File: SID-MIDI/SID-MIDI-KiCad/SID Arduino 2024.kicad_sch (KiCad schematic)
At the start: 33 parts, among them J1 Power, J5 Audio, J9 MIDI, SW4 Reset, SW6 Unison/Poly/Separate, U1 TL072, U2 6N138, U3 MOS6581/6582/8580SID

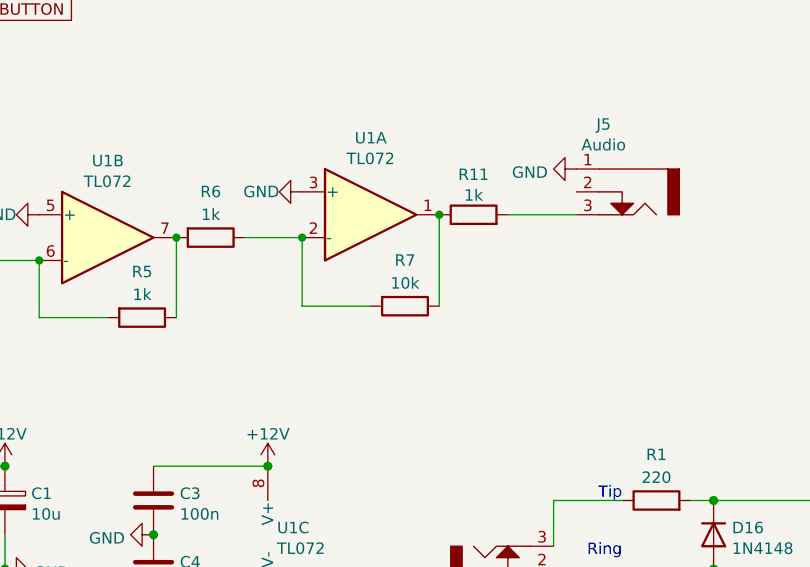
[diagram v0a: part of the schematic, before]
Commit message: Change amplification resistor to 1k8 to avoid clipping
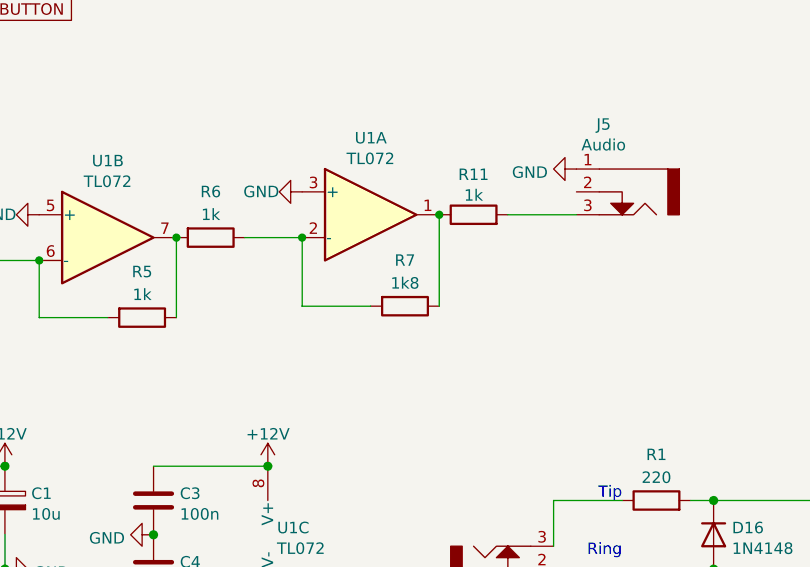
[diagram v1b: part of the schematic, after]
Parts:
- R7: value 10k -> 1k8
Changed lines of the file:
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@@
       (effects (font (size 1.27 1.27)))
     )
-    (property "Value" "10k" (at 88.9 147.32 90)
+    (property "Value" "1k8" (at 88.9 147.32 90)
       (effects (font (size 1.27 1.27)))
     )

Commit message: Add files via upload
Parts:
- R7: value 1k8 -> 1k
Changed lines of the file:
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@@
       (effects (font (size 1.27 1.27)))
     )
-    (property "Value" "1k8" (at 88.9 147.32 90)
+    (property "Value" "1k" (at 88.9 147.32 90)
       (effects (font (size 1.27 1.27)))
     )

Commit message: Add files via upload
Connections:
- net Poly/Unison 0: now also A1.1 (D1/TX); no longer A1.15 (D12)
- net SID DATA 1: now also A1.15 (D12); no longer A1.1 (D1/TX)
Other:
- note added: "The AMS1117 5.0V on the Arduino Nano should be able to supply at least 800mA, and the SID should draw about 100mA via Vcc, so this should be within safe limits, although the AMS1117 can get quite warm"
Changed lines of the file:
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@@
     (effects (font (size 1.27 1.27)) (justify right bottom))
+  )
+  (text "The AMS1117 5.0V on the Arduino Nano\nshould be able to supply at least 800mA,\nand the SID should draw about 100mA\nvia Vcc, so this should be within safe\nlimits, although the AMS1117 can get quite warm"
+    (at 166.37 49.53 0)
+    (effects (font (size 1.27 1.27)) (justify left bottom))
   )
   (text "D13: Important note:\nRemove resistor or LED from\nD13, to allow INPUT_PULLUP\nto work correctly"
@@
     )
   )
-  (global_label "Poly{slash}Unison 0" (shape input) (at 74.93 62.23 180) (fields_autoplaced)
-    (effects (font (size 1.27 1.27)) (justify right))
-    (property "Intersheetrefs" "${INTERSHEET_REFS}" (at 57.9593 62.23 0)
+  (global_label "Poly{slash}Unison 0" (shape input) (at 74.93 34.29 180) (fields_autoplaced)
+    (effects (font (size 1.27 1.27)) (justify right))
+    (property "Intersheetrefs" "${INTERSHEET_REFS}" (at 57.9593 34.29 0)
       (effects (font (size 1.27 1.27)) (justify right) hide)
     )
@@
     )
   )
-  (global_label "SID DATA 1" (shape input) (at 74.93 34.29 180) (fields_autoplaced)
-    (effects (font (size 1.27 1.27)) (justify right))
-    (property "Intersheetrefs" "${INTERSHEET_REFS}" (at 61.2853 34.29 0)
-      (effects (font (size 1.27 1.27)) (justify right) hide)
-    )
+  (global_label "SID DATA 1" (shape input) (at 74.93 62.23 180) (fields_autoplaced)
+    (effects (font (size 1.27 1.27)) (justify right))
+    (property "Intersheetrefs" "${INTERSHEET_REFS}" (at 61.2853 62.23 0)
+      (effects (font (size 1.27 1.27)) (justify right) hide)
+    )
